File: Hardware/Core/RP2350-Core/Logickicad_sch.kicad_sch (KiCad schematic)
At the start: 46 parts, among them J7 SWD, Q1 BSS123, Q3 BSS123, SW1 TS-1187A-B-A-B, SW2 TS-1187A-B-A-B, U1 RP2354B, U19 W25Q16JVSNIQ, U2 AP2112K-3.3, U3 LM66200DRLR, Y1 Crystal

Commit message: Verison RP2350 with arduino header support
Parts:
- removed Q1, Q3: BSS123, SpaghettiLAB:SOT-23-3_L2.9-W1.5-P1.90-LS2.6-BR, symbol Transistor_FET:BSS123
- removed U1: RP2354B, SpaghettiLAB:QFN-80_L10.0-W10.0-P0.40-TL-EP3.4, symbol MCU_RaspberryPi:RP2354B
- removed USBC1: TYPE-C-31-M-14, SpaghettiLAB:USB-C-SMD_12P-P0.50-H-F_TYPE-C-31-M-14, symbol SpaghettiLab:TYPE-C-31-M-14
- added Q2, Q3: 2N7002, SpaghettiLAB:SOT-23-3_L2.9-W1.3-P1.90-LS2.4-BR, symbol Transistor_FET:2N7002
- added U4: RP2350A, SpaghettiLAB:QFN-60_L7.0-W7.0-P0.40-TL-EP3.4, symbol MCU_RaspberryPi:RP2350A
- added USB1: TYPEC-324G-BCP24, SpaghettiLAB:USB-C-SMD_TYPEC-324G-BCP24, symbol SpaghettiLAB:TYPEC-324G-BCP24
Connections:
- net +1V1: now also U4.23 (DVDD), U4.39 (DVDD), U4.50 (VREG_FB), U4.6 (DVDD)
- net +3V3: now also U4.1 (IOVDD), U4.11 (IOVDD), U4.20 (IOVDD), U4.30 (IOVDD), U4.38 (IOVDD), U4.44 (ADC_AVDD), U4.45 (IOVDD), U4.49 (VREG_VIN), U4.53 (USB_OTP_VDD), U4.54 (QSPI_IOVDD)
- net ADD_LED: now also Q2.1 (G), U4.5 (GPIO3)
- net FLEX0: now also U4.14 (GPIO10)
- net FLEX1: now also U4.15 (GPIO11)
- net FLEX2: now also U4.43 (GPIO29/ADC3)
- net FLEX3: now also U4.40 (GPIO26/ADC0)
- net FLEX4: now also U4.41 (GPIO27/ADC1)
- net FLEX5: now also U4.42 (GPIO28/ADC2)
- net FLEX6: now also U4.16 (GPIO12)
- net GND: now also Q2.2 (S), Q3.2 (S), U4.47 (VREG_PGND), U4.61 (GND), USB1.1 (EP), USB1.2 (EP), USB1.3 (EP), USB1.4 (EP)
- net GPIO0: now also U4.2 (GPIO0)
- net GPIO1: now also U4.3 (GPIO1)
- net GPIO13: now also U4.17 (GPIO13)
- net GPIO14: now also U4.18 (GPIO14)
- net GPIO15: now also U4.19 (GPIO15)
- net GPIO18: now also U4.29 (GPIO18)
- net GPIO19: now also U4.31 (GPIO19)
- net GPIO2: now also U4.4 (GPIO2)
- net GPIO20: now also U4.32 (GPIO20)
- net GPIO21: now also U4.33 (GPIO21)
- net GPIO22: now also U4.34 (GPIO22)
- net GPIO23: now also U4.35 (GPIO23)
- net GPIO24: now also U4.36 (GPIO24)
- net GPIO4: now also U4.7 (GPIO4)
- net ID: now also U4.13 (GPIO9)
- net PS_EN: now also Q3.3 (D)
- net PWR_SOURCE_ST: now also U4.37 (GPIO25)
- net QSPI_SCLK: now also U4.56 (QSPI_SCLK)
- net QSPI_SD0: now also U4.57 (QSPI_SD0)
- net QSPI_SD1: now also U4.59 (QSPI_SD1)
- net QSPI_SD2: now also U4.58 (QSPI_SD2)
- net QSPI_SD3: now also U4.55 (QSPI_SD3)
- net QSPI_SS: now also U4.60 (~{QSPI_SS})
- net SCL_ALT: now also U4.10 (GPIO7)
- net SCL_AUX: now also U4.28 (GPIO17)
- net SDA_ALT: now also U4.9 (GPIO6)
- net SDA_AUX: now also U4.27 (GPIO16)
- net SIO: now also U4.25 (SWDIO)
- net SWC: now also U4.24 (SWCLK)
- net USB_CC1: now also USB1.A5 (CC1)
- net USB_CC2: now also USB1.B5 (CC2)
- net USB_DM: now also USB1.A7 (DN1), USB1.B7 (DN2)
- net USB_DP: now also USB1.A6 (DP1), USB1.B6 (DP2)
- net VBUS: now also USB1.A4 (VBUS), USB1.A9 (VBUS), USB1.B4 (VBUS), USB1.B9 (VBUS)
- net VLOGIC: now also Q3.1 (G)
- net VREG_LX: now also U4.48 (VREG_LX)
- net ~{INT}: now also U4.8 (GPIO5)
- net ~{RESET}: now also U4.12 (GPIO8), U4.26 (RUN)
- net at C5.2, Y1.3: now also U4.21 (XIN)
- net at R46.2: now also U4.52 (USB_DP)
- net at C26.1, R23.1: now also U4.46 (VREG_AVDD)
- net at R49.1: now also U4.22 (XOUT)
- net at R47.2: now also U4.51 (USB_DM)
- net at R42.2: now also Q2.3 (D)
- no-connect marks 11 -> 19
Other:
- moved on the sheet: C58, D1, R30, R42, TP4, U19

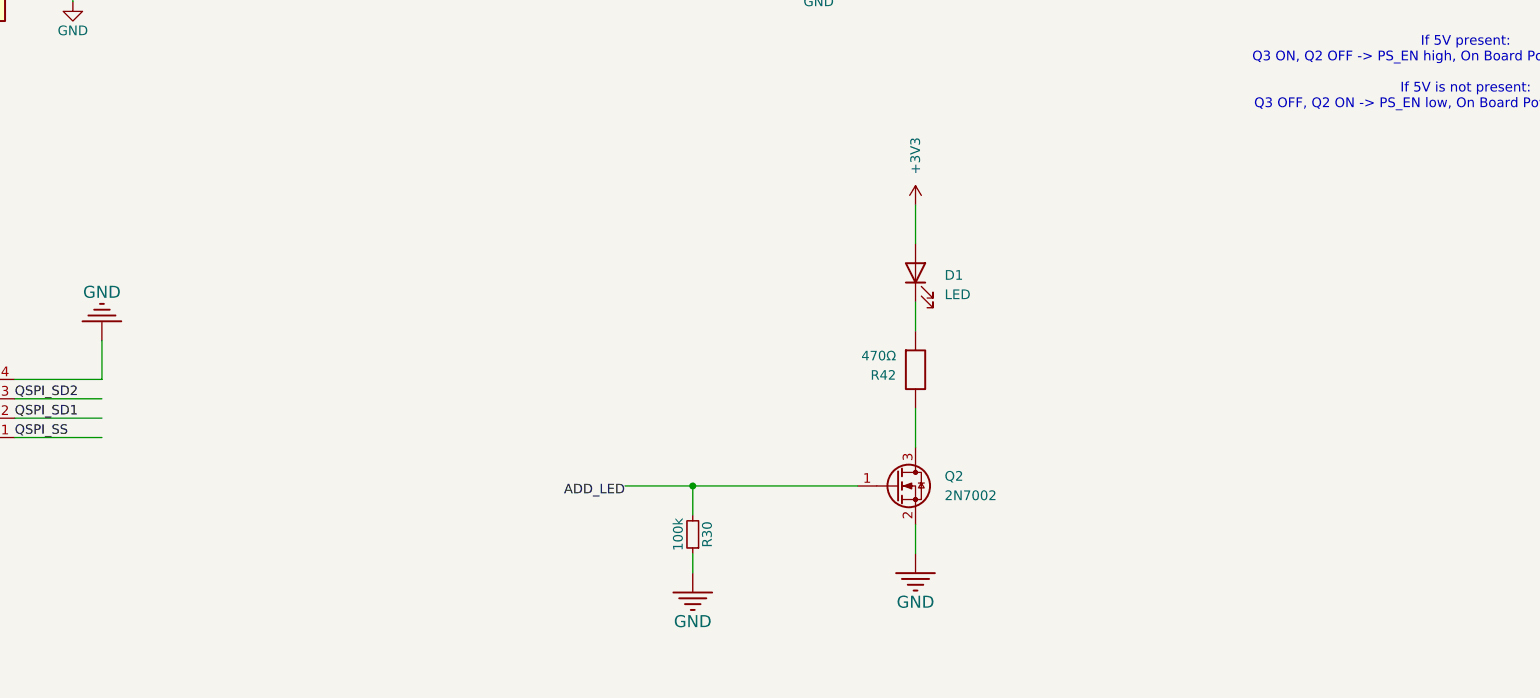
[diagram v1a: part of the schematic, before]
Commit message: Added ADC TI ADS1115IDGSR to match arduino pinout and function and isolate arduino connections from spaghetti bus
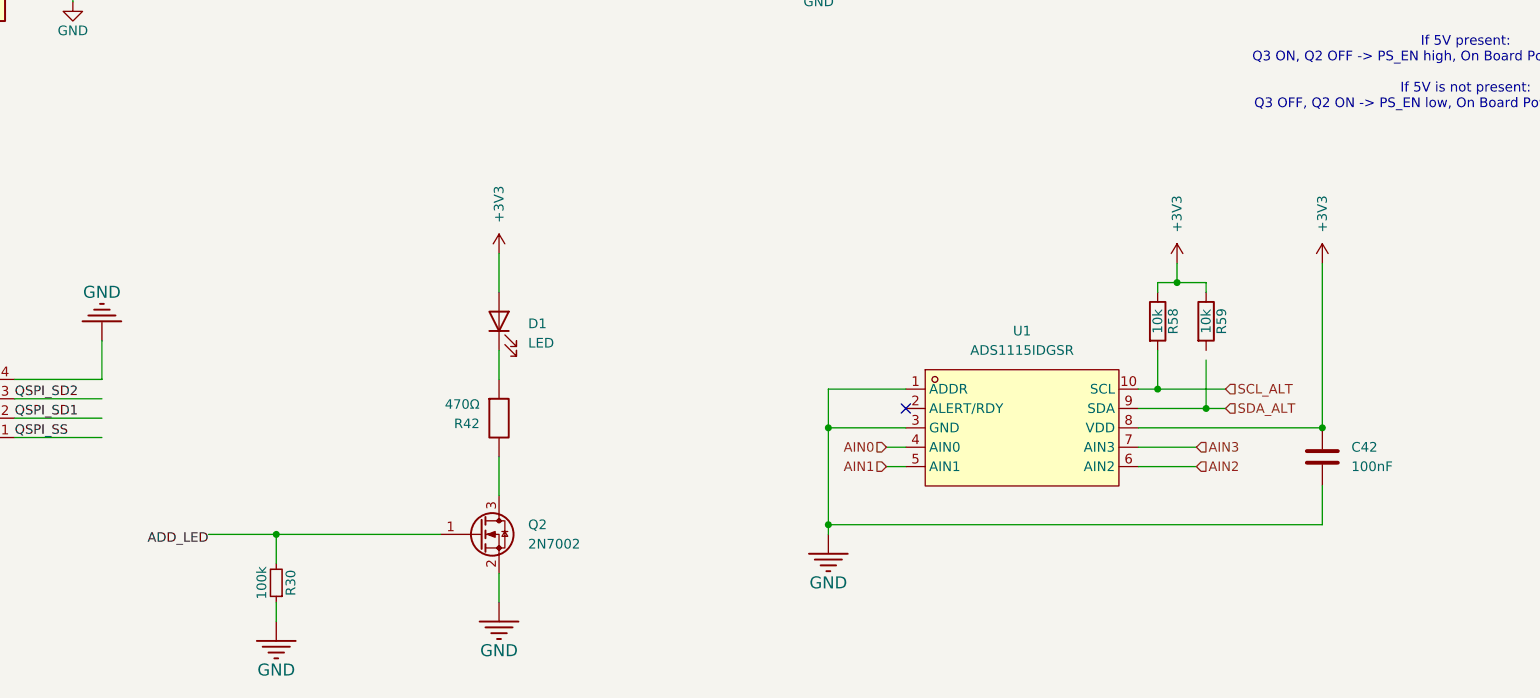
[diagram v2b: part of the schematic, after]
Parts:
- added C42: 100nF, SpaghettiLAB:C0603, symbol Device:C
- added R58, R59: 10k, SpaghettiLAB:R0603, symbol Device:R
- added U1: ADS1115IDGSR, SpaghettiLAB:MSOP-10_L3.0-W3.0-P0.50-LS5.0-BL, symbol SpaghettiLAB:ADS1115IDGSR
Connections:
- net +3V3: now also C42.2, R58.1, R59.1, U1.8 (VDD)
- net GND: now also C42.1, U1.1 (ADDR), U1.3 (GND)
- net SCL_ALT: now also R58.2, U1.10 (SCL)
- net SDA_ALT: now also U1.9 (SDA)
- new net AIN0: U1.4 (AIN0)
- new net AIN1: U1.5 (AIN1)
- new net AIN2: U1.6 (AIN2)
- new net AIN3: U1.7 (AIN3)
- no-connect marks 19 -> 20
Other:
- moved on the sheet: D1, Q2, R30, R42

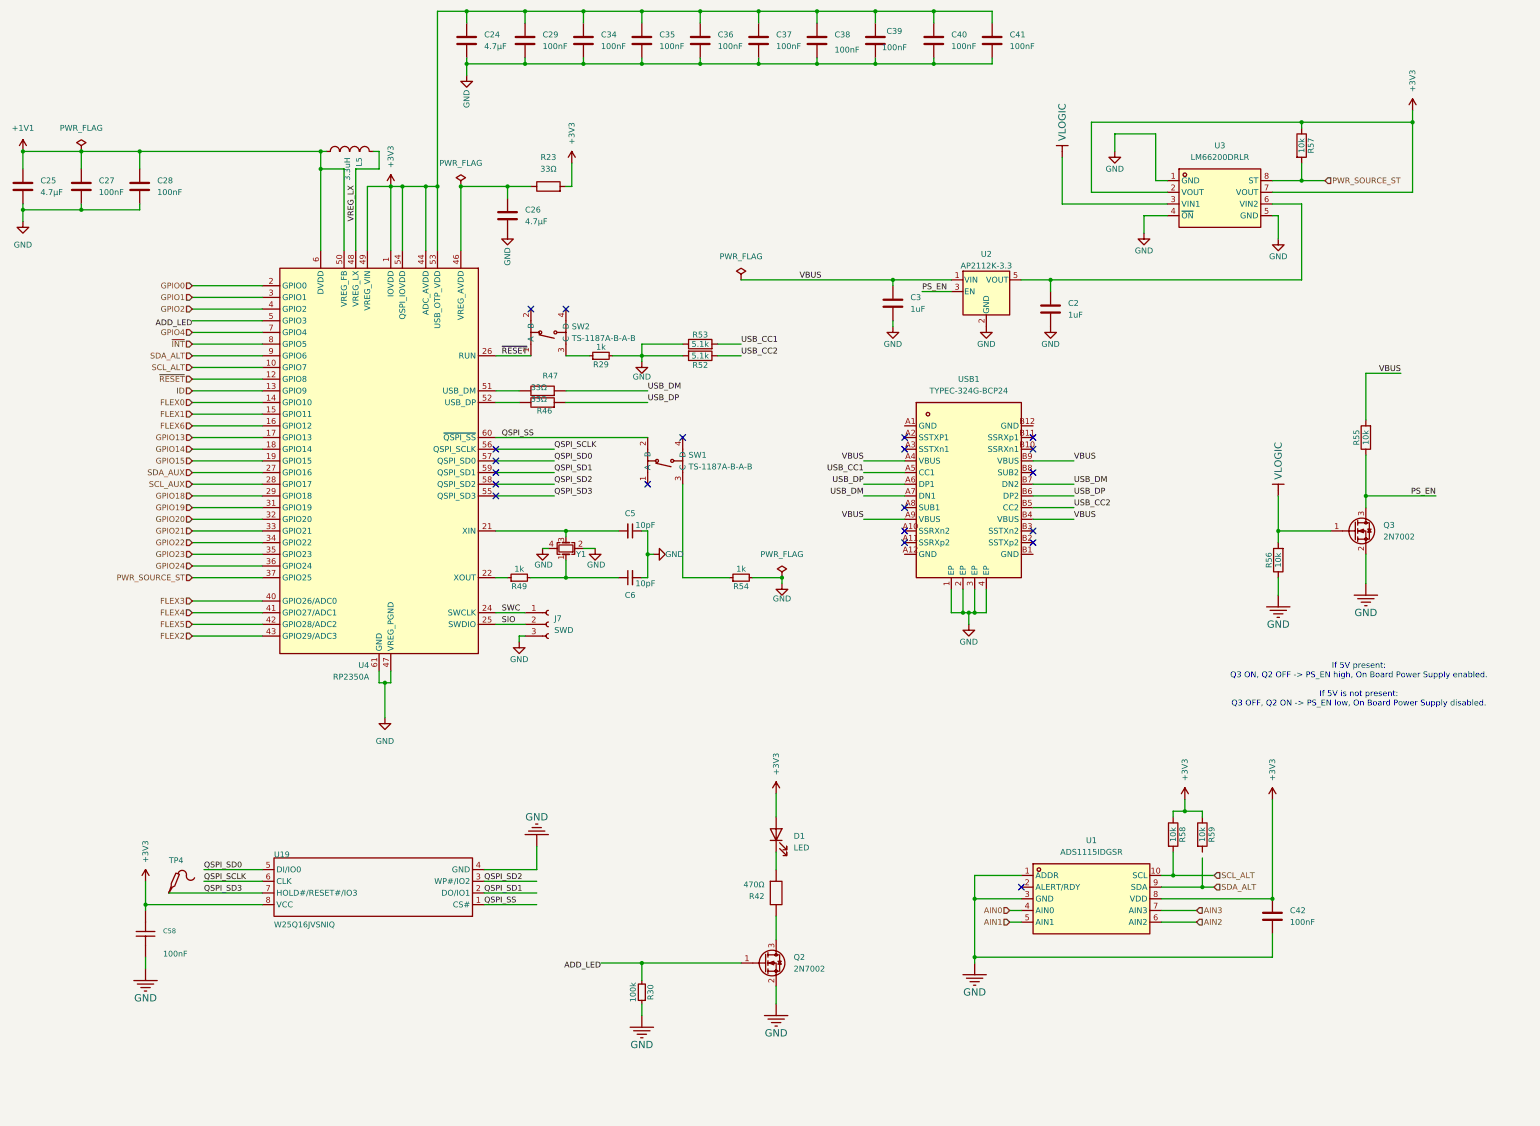
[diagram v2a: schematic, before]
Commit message: Placed footprints RP235x
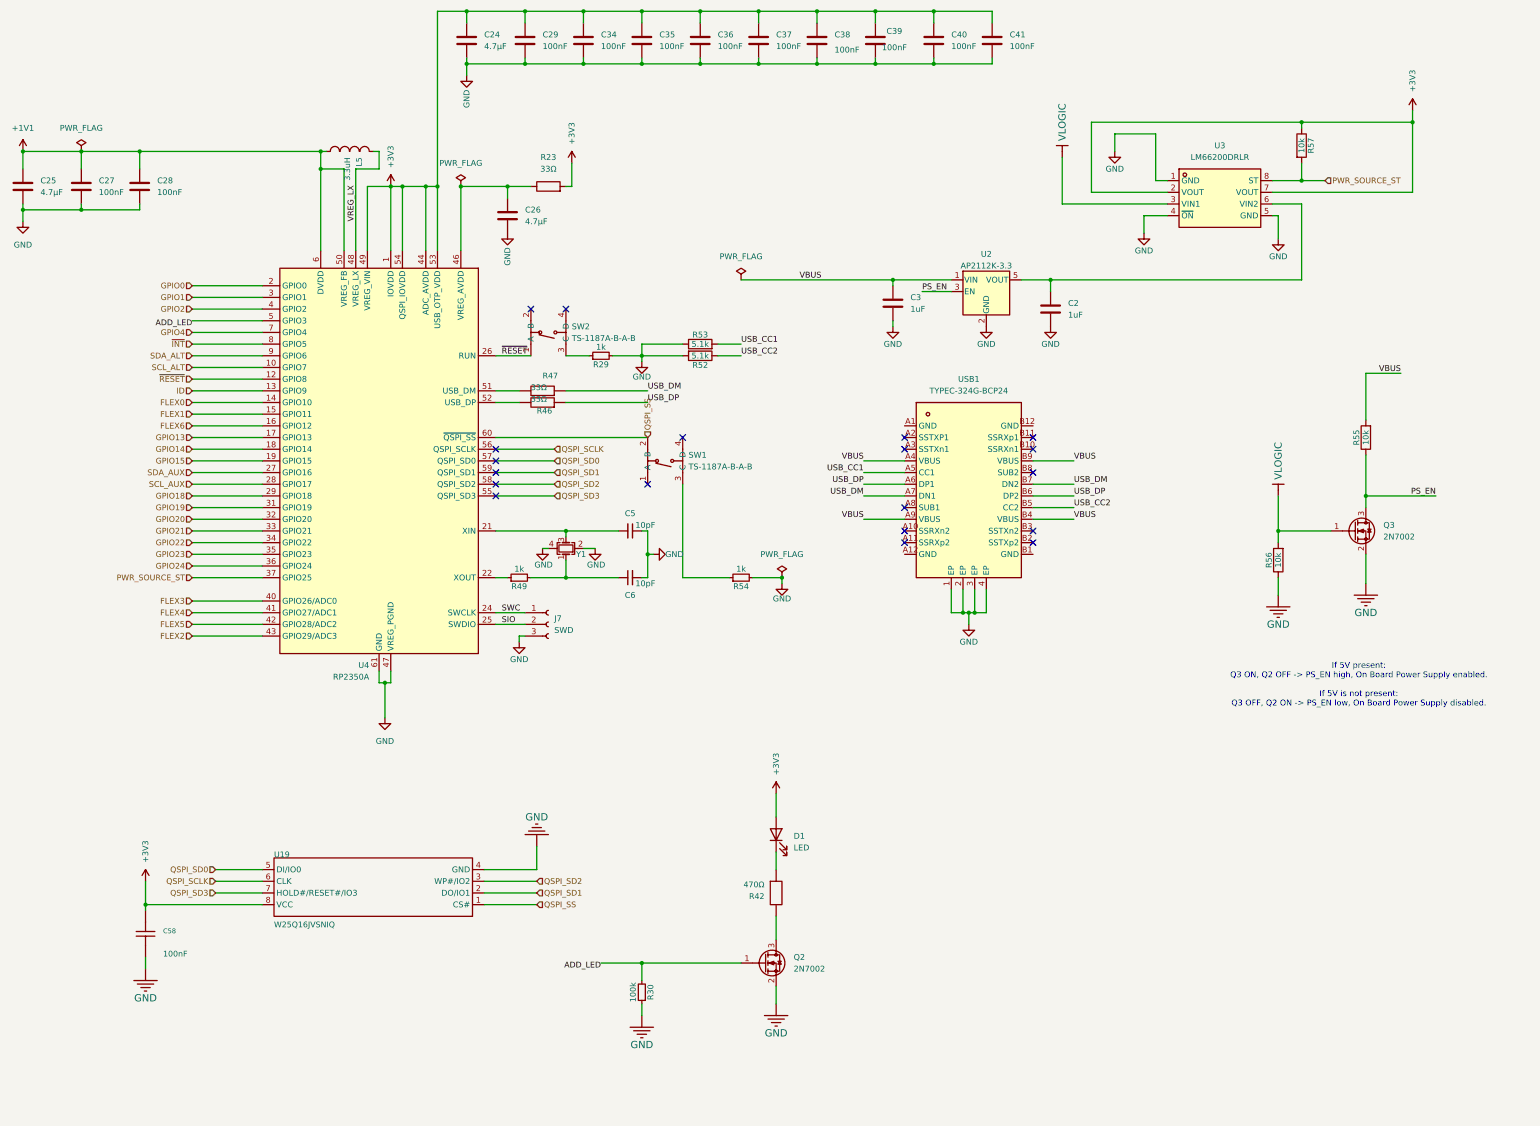
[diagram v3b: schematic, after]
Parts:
- removed C42: 100nF, SpaghettiLAB:C0603, symbol Device:C
- removed R58, R59: 10k, SpaghettiLAB:R0603, symbol Device:R
- removed TP4: (no value), TestPoint:TestPoint_Pad_D2.5mm, symbol USBC_PD_mo-easyedapro:Test-Point
- removed U1: ADS1115IDGSR, SpaghettiLAB:MSOP-10_L3.0-W3.0-P0.50-LS5.0-BL, symbol SpaghettiLAB:ADS1115IDGSR
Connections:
- no-connect marks 20 -> 19
